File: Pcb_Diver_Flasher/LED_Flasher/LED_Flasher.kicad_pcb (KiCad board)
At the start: 2 copper layers, 105 x 20 mm, 24 parts, among them IC100 PIC16LF15313, IC101 MP3217, J100 SKEDD6, SW100 MK15-C2, T100 MJD122T4

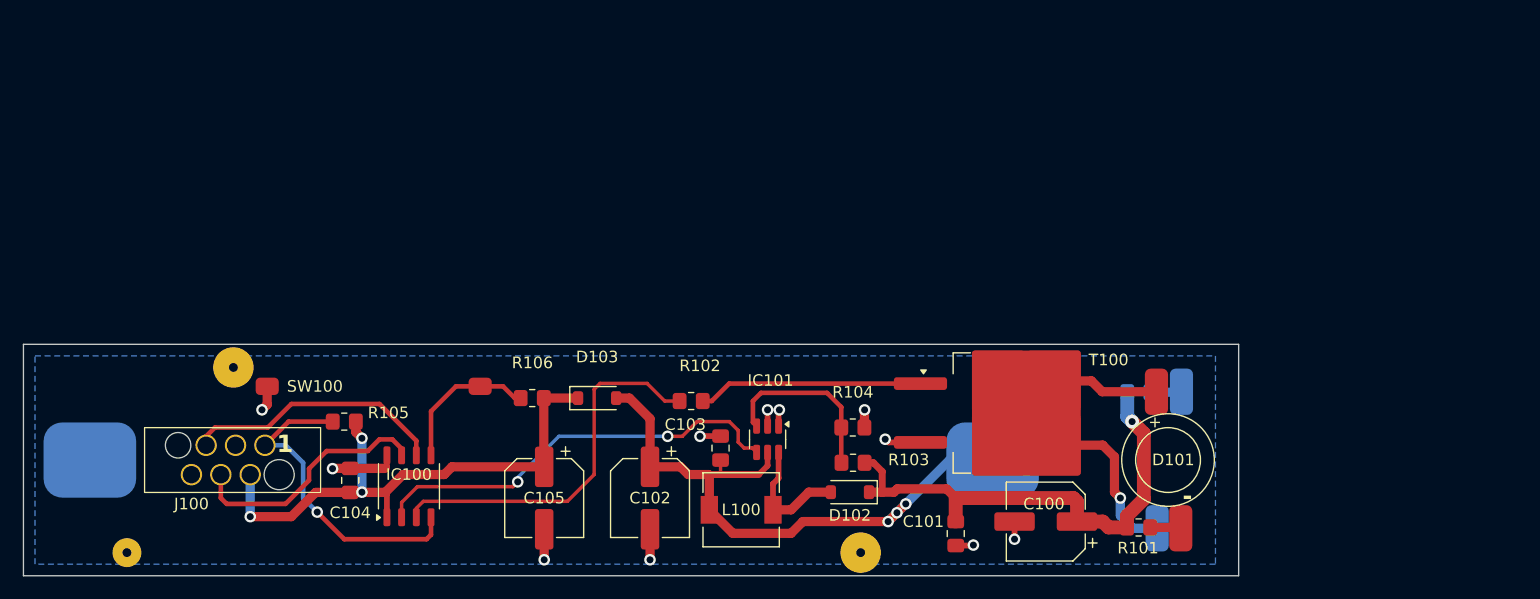
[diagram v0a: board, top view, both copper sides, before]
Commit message: Started with version 1.1 of the dive flasher PCB. 1.0 => old too weak booster 1.1 => new hopefully more powerful booster
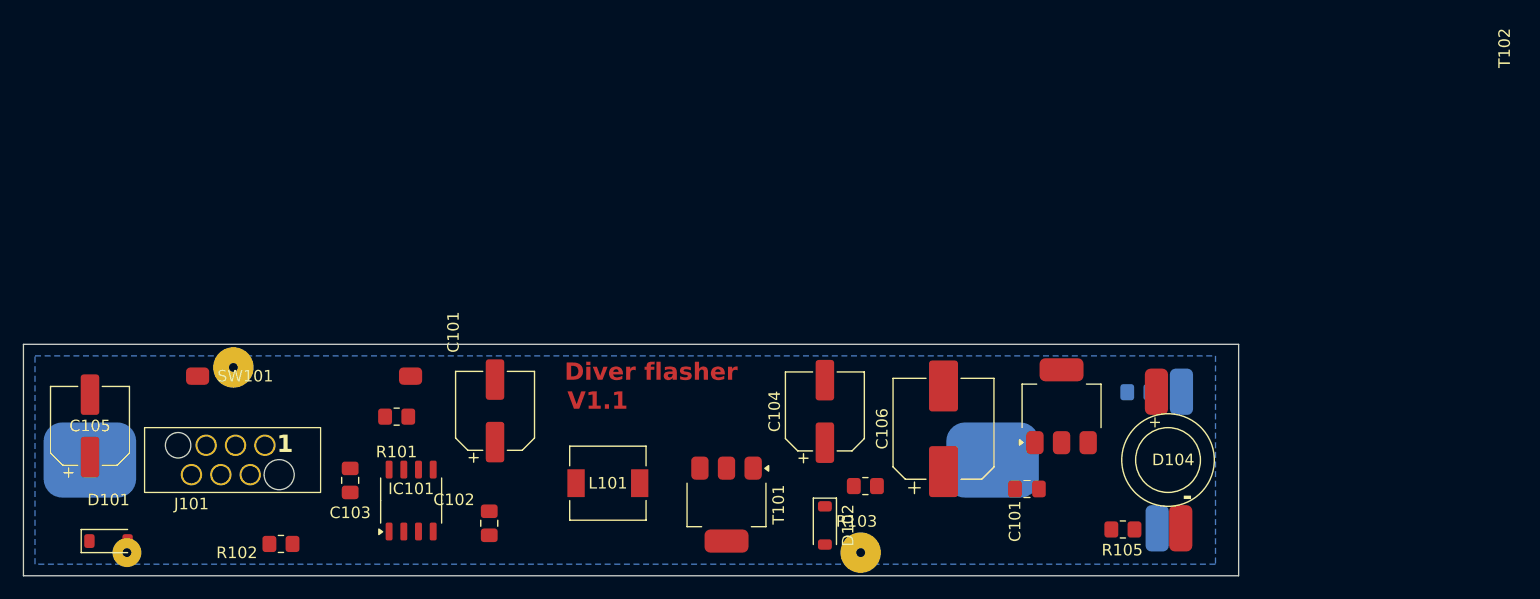
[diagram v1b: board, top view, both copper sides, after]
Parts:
- removed the C102 at (104.1, 113.3)
- removed the IC101 at (114.3, 108.2)
- removed the R103 at (121.7, 110.2)
- removed the R104 at (121.7, 107.2)
- removed T100: MJD122T4, Package_TO_SOT_SMD:TO-263-2
- added C101: 100µF/10V, Capacitor_SMD:CP_Elec_6.3x7.7, F.Cu at (90.8, 105.8)
- added C104: 100µF/10V, Capacitor_SMD:CP_Elec_6.3x7.7, F.Cu at (119.2, 105.8)
- added T101: BUK7880-55A, Package_TO_SOT_SMD:SOT-223-3_TabPin2, F.Cu at (110.8, 113.8)
- added T102: BUK7880-55A, Package_TO_SOT_SMD:SOT-223-3_TabPin2, F.Cu at (139.7, 105.3)
- C106: renamed from C100; footprint Capacitor_SMD:CP_Elec_6.3x7.7 -> Capacitor_SMD:CP_Elec_8x10.5
- D103: renamed from D100; value LB-P200W2C60 -> LB-P200W2C-H3
- D104: renamed from D101; value LB-P200W2C60 -> LB-P200W2C-H3
- L101: renamed from L100; value 33µH -> 330µH
- R103: renamed from R102; value 1K -> 0.68
- R104: renamed from R100; value 1 -> 0.47
- R105: renamed from R101; value 1 -> 0.47
- moved D101 44.0 mm to (57.4, 117.0)
- moved C105 39.7 mm to (55.8, 107.0), turned to 90 degrees
- moved C102 21.0 mm to (90.2, 115.5)
- moved R103 16.8 mm to (122.8, 112.2), turned to 180 degrees
- moved C106 11.9 mm to (129.5, 107.3), turned to 90 degrees
- moved R102 11.9 mm to (72.2, 117.2), turned to 0 degrees
- moved R101 11.8 mm to (82.2, 106.2), turned to 0 degrees
- moved L101 11.7 mm to (100.5, 112.0)
- moved C101 7.26 mm to (136.7, 112.5), turned to 0 degrees
- moved SW101 6.08 mm to (74.2, 102.8)
- moved D102 3.60 mm to (119.2, 115.7), turned to -90 degrees
- moved R105 1.37 mm to (145.0, 116.0)
- moved IC101 1.25 mm to (83.5, 113.5)
- renumbered BAT100 to BAT101, C103 to C102, C104 to C103, D103 to D101, IC100 to IC101, J100 to J101, R106 to R101, R105 to R102, SW100 to SW101
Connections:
- net /Battery_Power renamed +BATT
- net /SW renamed /SW_OUT
- D102 pad 1: /LED_PWR -> Net-(D102-K)
- IC101 pad 2: 5V_EN -> SW_IN
- R103 pad 1: Flash_on -> /LED_PWR
- R103 pad 2: /BT100 -> Net-(D102-K)
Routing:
- net +BATT: track 52.0 -> 0.00 mm, vias 3 -> 0
- net /PWR_MCU: track 48.2 -> 0.00 mm, vias 3 -> 0
- net /LED_PWR: track 43.3 -> 0.00 mm, vias 1 -> 0
- net 5V_EN: track 37.1 -> 0.00 mm, vias 2 -> 0
- net Flash_on: track 32.9 -> 0.00 mm
- net /MCLR!: track 27.9 -> 0.00 mm, vias 1 -> 0
- net GND: track 25.7 -> 0.00 mm, vias 11 -> 0
- net Net-(D103-K): track 23.7 -> 0.00 mm, vias 1 -> 0
- net /ICSPCLK: track 22.7 -> 0.00 mm
- net /ICSPDAT: track 21.7 -> 0.00 mm
- net /BT100: track 19.4 -> 0.00 mm
- net /FB: track 15.6 -> 0.00 mm
- net /Reed: track 12.9 -> 0.00 mm
- net /SW_OUT: track 10.8 -> 0.00 mm
- net /A1: track 2.70 -> 0.00 mm
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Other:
- board text added: "Diver flasher"
- board text added: "V1.1"

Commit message: Start with next version "home brew" boost converter
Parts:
- C106: footprint Capacitor_SMD:CP_Elec_8x10.5 -> Capacitor_SMD:CP_Elec_6.3x7.7
